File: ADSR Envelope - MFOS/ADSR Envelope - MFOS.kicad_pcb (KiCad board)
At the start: 2 copper layers, 101.6 x 76.2 mm, 65 parts, among them J1 Trig_In, J10 SUS3, J11 ADSR_OUT, J12 Manual_Gate, J13 +12V_Conn, J14 -12V_Conn, J15 GND_Conn, J2 Gate_In, J3 APT, J4 RPT, J5 PCM, J6 DPT, J7 TSW, J8 SUS2, J9 ADSR, U1 4066, U2 TL082, U3 CD40106, U4 TL084, U5 4001

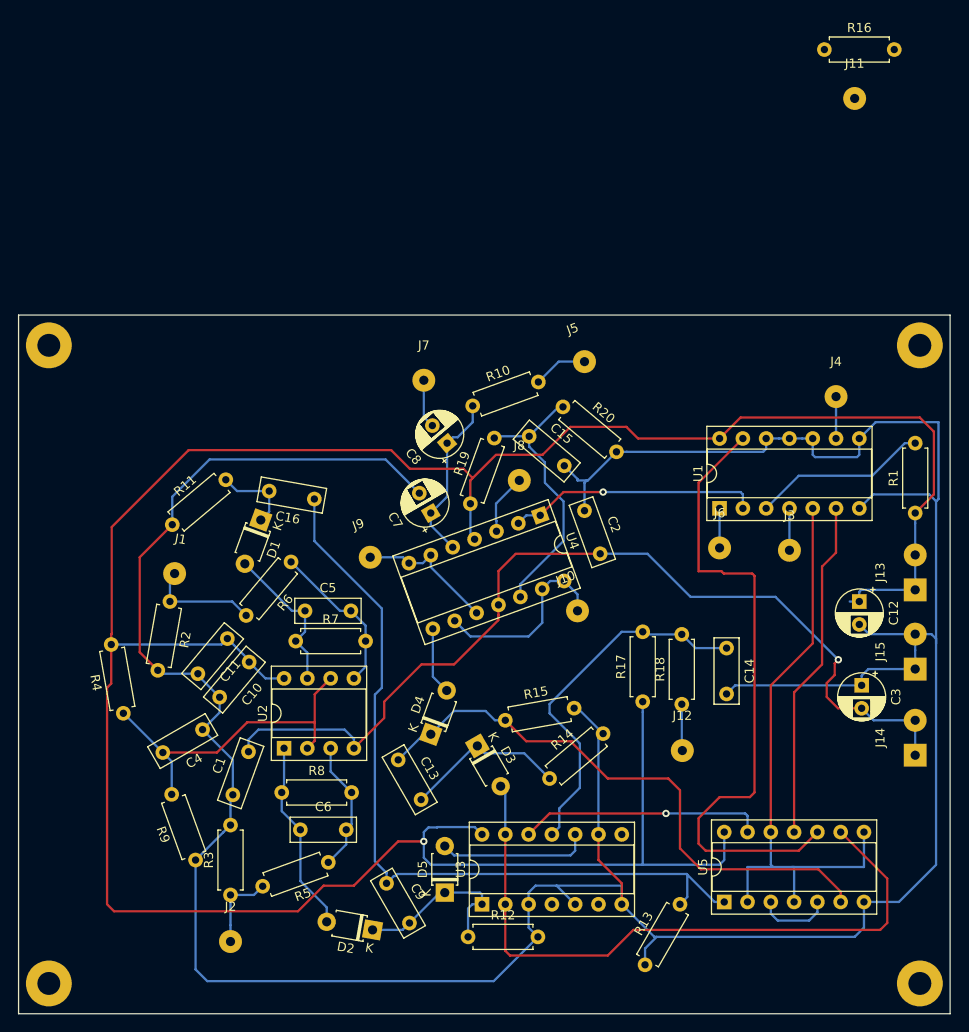
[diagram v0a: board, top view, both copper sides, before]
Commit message: silkscreen designators placed
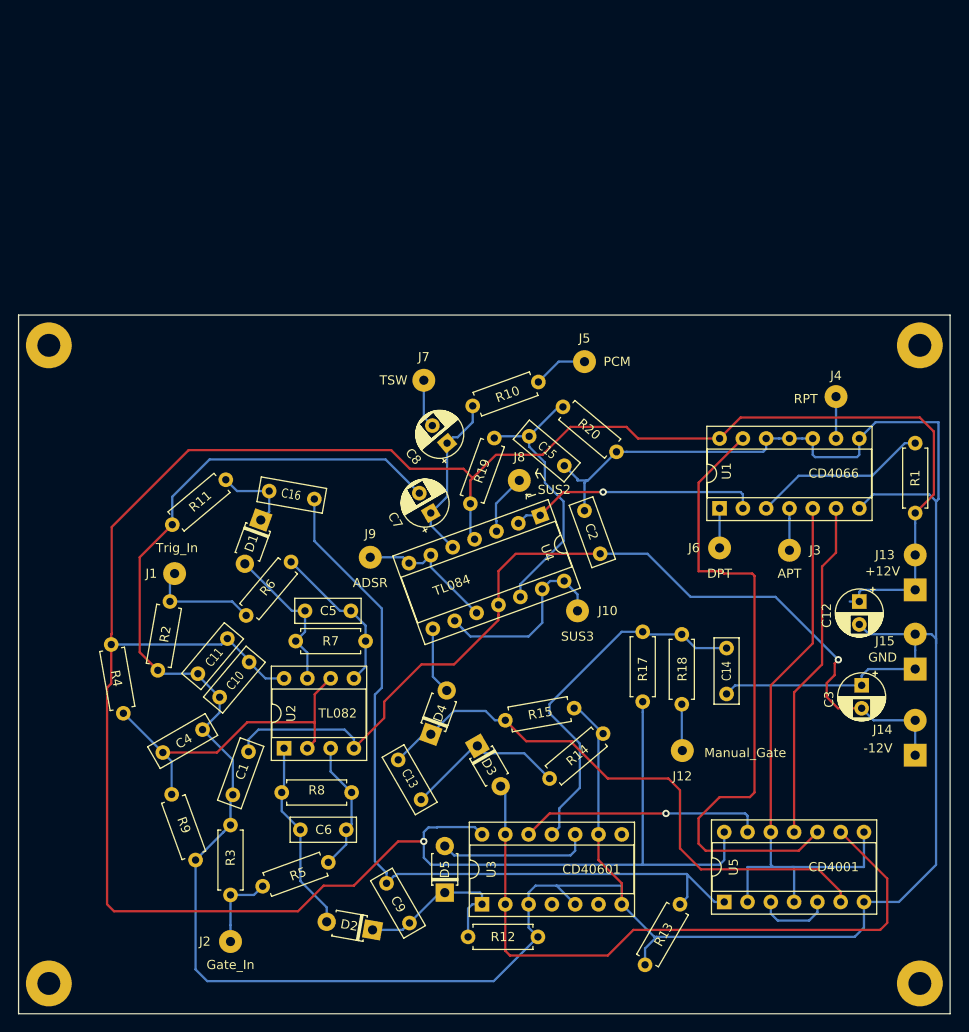
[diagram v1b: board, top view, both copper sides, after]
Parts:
- removed J11: ADSR_OUT, Connector_Wire:SolderWirePad_1x01_Drill1mm
- removed R16: 1K, Resistor_THT:R_Axial_DIN0207_L6.3mm_D2.5mm_P7.62mm_Horizontal
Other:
- net class Default: clearance 0.2 -> 0.5
- rule trace_clearance: 0.2 -> 0.5
- rule via_min_size: 0.4 -> 0.6
- board text added: "+12V"
- board text added: "-12V"
- board text added: "ADSR"
- board text added: "APT"
- board text added: "CD4001"
- board text added: "CD40601"
- board text added: "CD4066"
- board text added: "DPT"
- board text added: "GND"
- board text added: "Gate_In"
- board text added: "Manual_Gate"
- board text added: "PCM"
- board text added: "RPT"
- board text added: "SUS2"
- board text added: "SUS3"
- board text added: "TL082"
- board text added: "TL084"
- board text added: "TSW"
- board text added: "Trig_In"

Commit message: doodled on silkscreen
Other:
- board text added: "MFOS"

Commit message: hiiiii
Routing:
- added copper zone on F.Cu, net (none)
- added copper zone on B.Cu, net Earth
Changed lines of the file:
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@@
   (page A4)
   (layers
-    (0 F.Cu signal)
+    (0 F.Cu signal hide)
     (31 B.Cu signal)
     (32 B.Adhes user hide)
@@
     (visible_elements FFFFFF7F)
     (pcbplotparams
-      (layerselection 0x010fc_ffffffff)
+      (layerselection 0x010e0_ffffffff)
       (usegerberextensions false)
       (usegerberattributes false)
@@
       (outputformat 1)
       (mirror false)
-      (drillshape 1)
+      (drillshape 0)
       (scaleselection 1)
       (outputdirectory ""))
@@
   (segment (start 94.234 77.47) (end 94.234 76.2) (width 0.25) (layer B.Cu) (net 40))
   (segment (start 94.996 78.232) (end 94.234 77.47) (width 0.25) (layer B.Cu) (net 40))
+  (zone (net 0) (net_name "") (layer F.Cu) (hatch edge 0.508)
+    (connect_pads (clearance 0.508))
+    (min_thickness 0.254)
+    (fill yes (arc_segments 32) (thermal_gap 0.508) (thermal_bridge_width 0.508))
+    (polygon
+      (pts
+        (xy 12.2 12.2) (xy 12.2 88.39) (xy 113.78 88.38) (xy 113.79 12.2)
+      )
+    )
+  )
+  (zone (net 1) (net_name Earth) (layer B.Cu) (hatch edge 0.508)
+    (connect_pads (clearance 0.508))
+    (min_thickness 0.254)
+    (fill yes (arc_segments 32) (thermal_gap 0.508) (thermal_bridge_width 0.508))
+    (polygon
+      (pts
+        (xy 12.2 12.2) (xy 12.2 88.37) (xy 113.79 88.39) (xy 113.79 12.19)
+      )
+    )
+  )
 )
